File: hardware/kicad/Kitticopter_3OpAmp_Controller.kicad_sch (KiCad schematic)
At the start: 25 parts, among them J1 DAQ interface, J2 Bench supply, P1 10k, U1 LM741, U2 LM741, U3 LM741

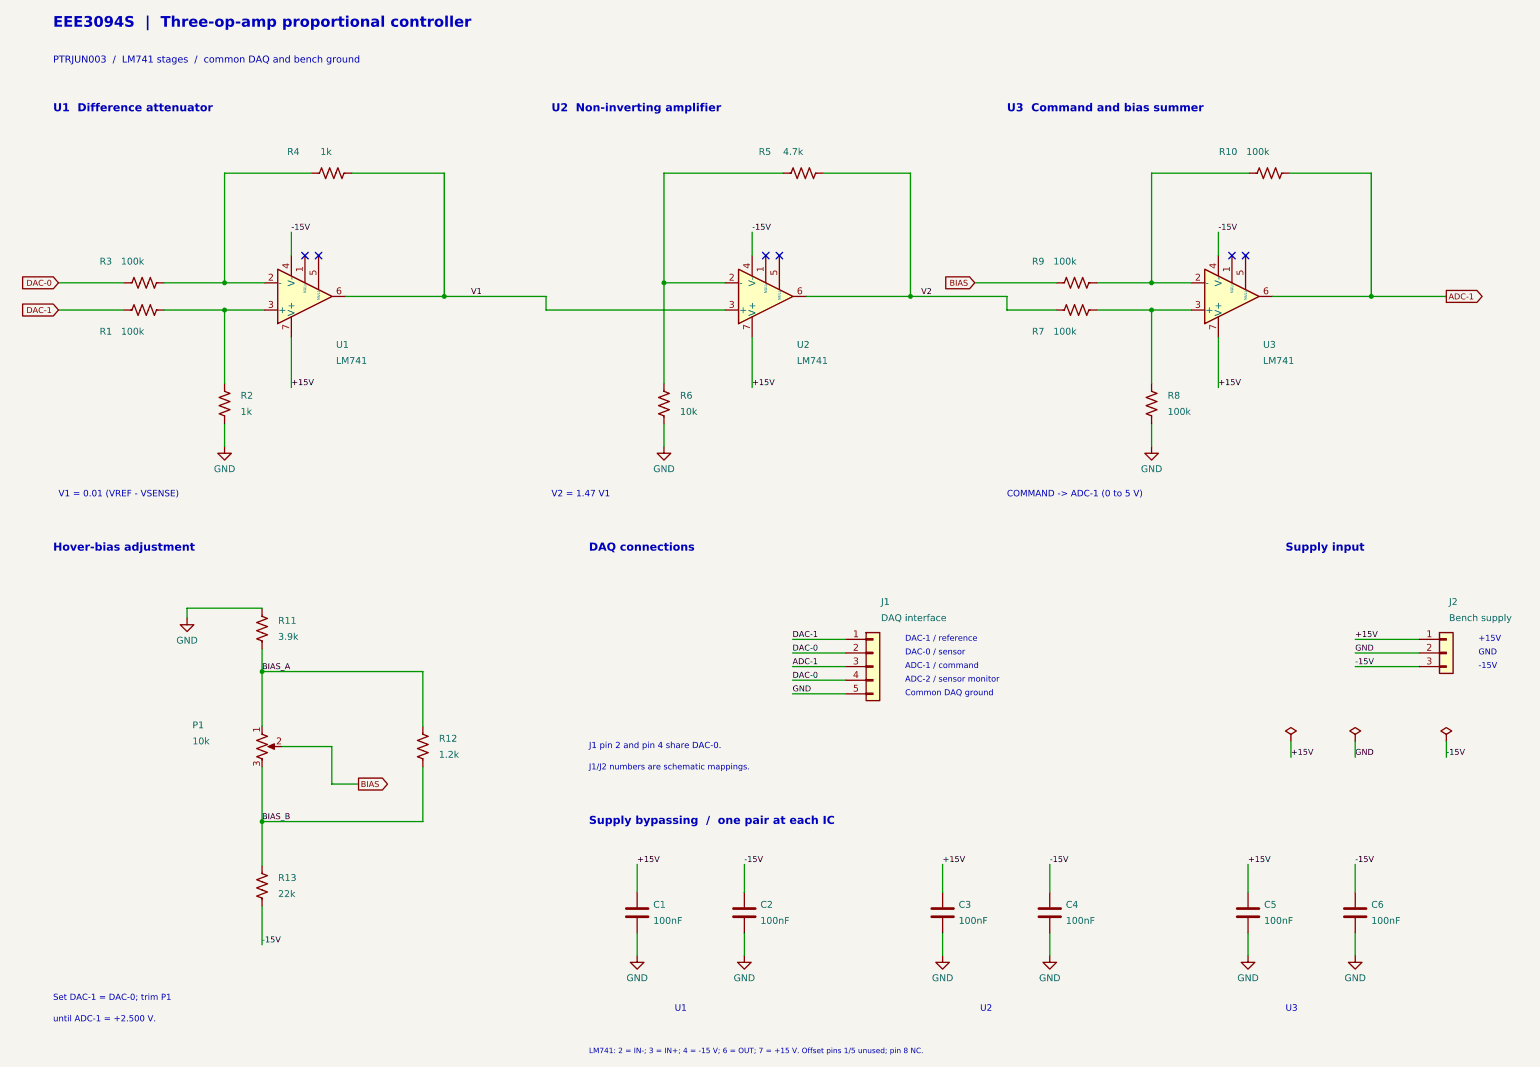
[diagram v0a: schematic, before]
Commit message: Revise 14-page report with linked Python/MATLAB plots, Simulink comparison and simplified KiCad circuit
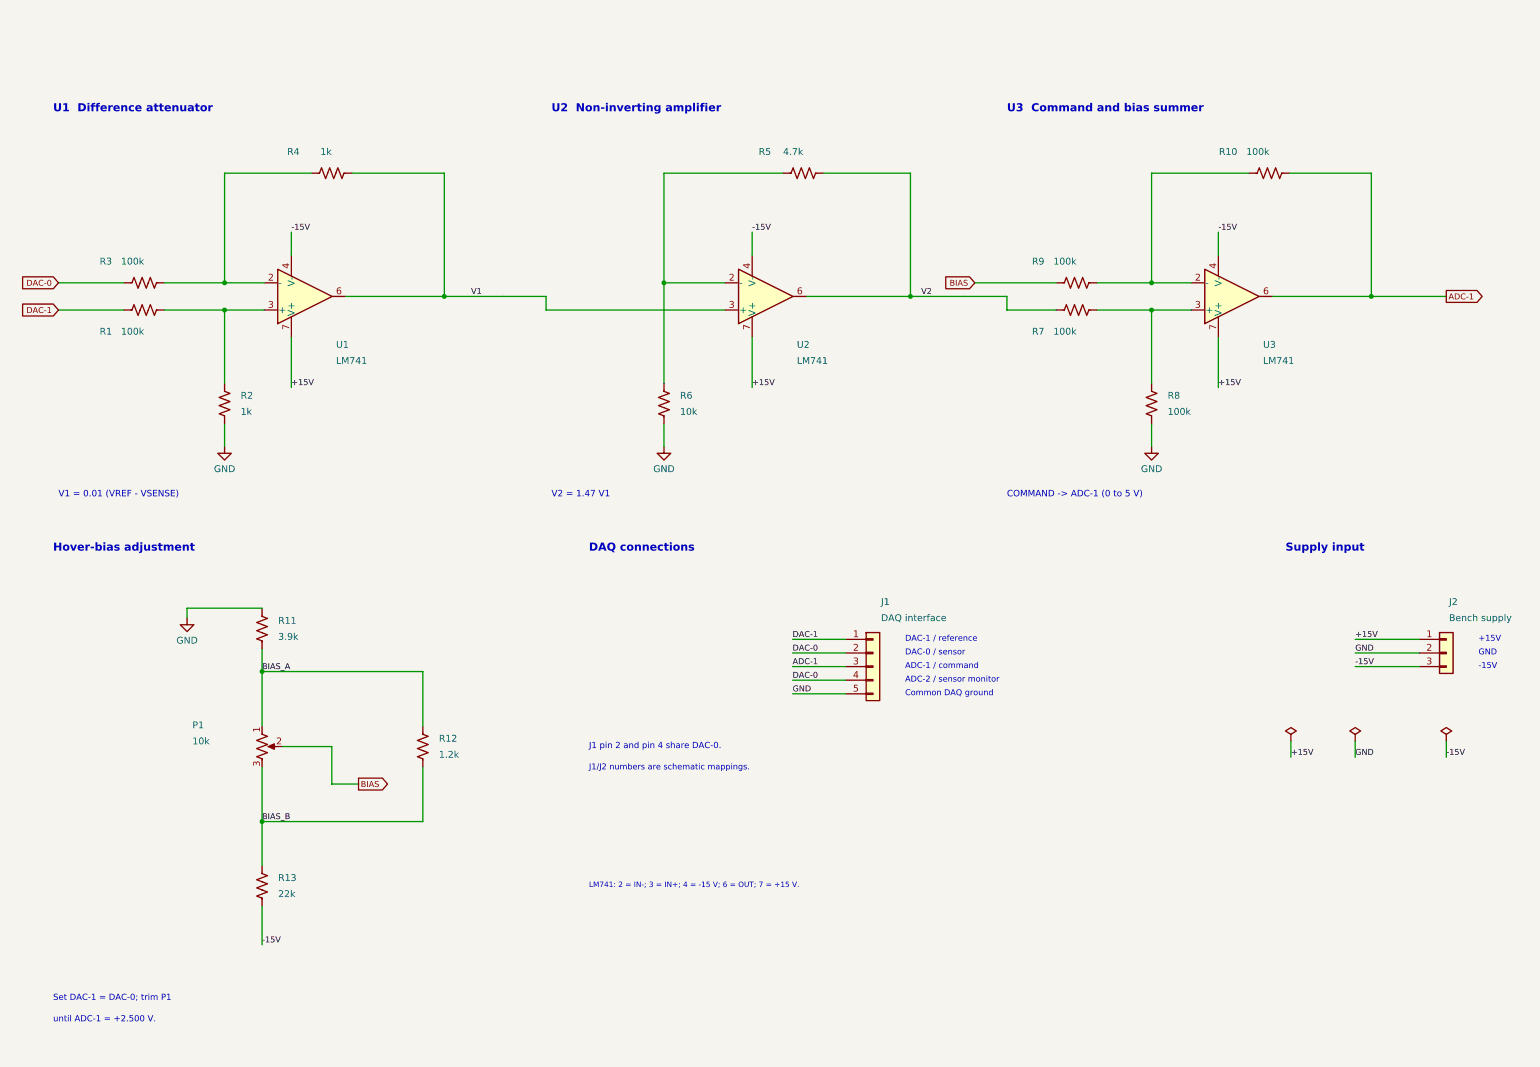
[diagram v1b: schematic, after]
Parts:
- removed C1, C2, C3, C4, C5, C6: 100nF, symbol Controller:C
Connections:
- no-connect marks 6 -> 0
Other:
- note added: "LM741: 2 = IN-; 3 = IN+; 4 = -15 V; 6 = OUT; 7 = +15 V."
- note removed: "EEE3094S | Three-op-amp proportional controller"
- note removed: "LM741: 2 = IN-; 3 = IN+; 4 = -15 V; 6 = OUT; 7 = +15 V. Offset pins 1/5 unused; pin 8 NC."
- note removed: "PTRJUN003 / LM741 stages / common DAQ and bench ground"
- note removed: "Supply bypassing / one pair at each IC"
- note removed: "U1"
- note removed: "U2"
- note removed: "U3"
